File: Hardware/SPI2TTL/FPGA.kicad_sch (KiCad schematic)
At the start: 98 parts, among them J1 Conn_01x06, J7 Conn_02x07_Odd_Even, J8 Conn_01x40, SW1 SW_Push, SW2 SW_Push, SW3 SW_Push, SW4 SW_DIP_x03, U1 XC7S15-2CSGA225I, U2 IS25LP032D, X1 SG-5032CBN

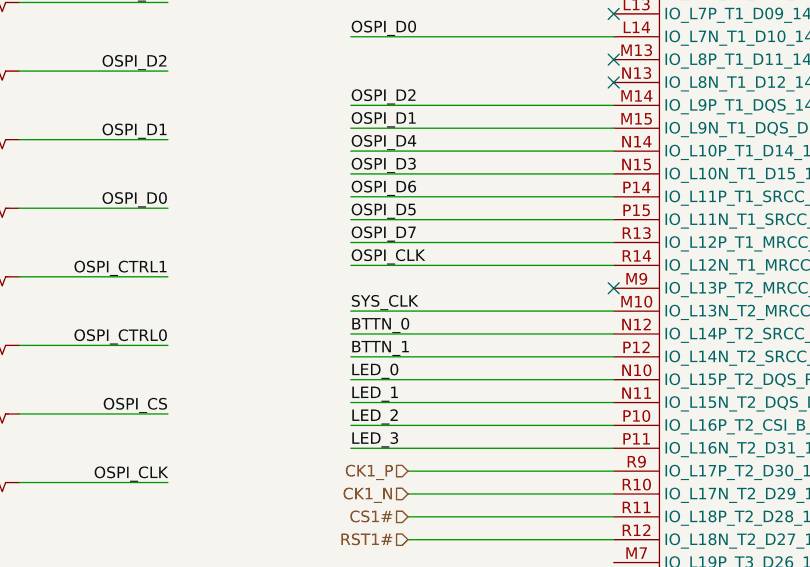
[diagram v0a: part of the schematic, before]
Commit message: Fixed CLK pins
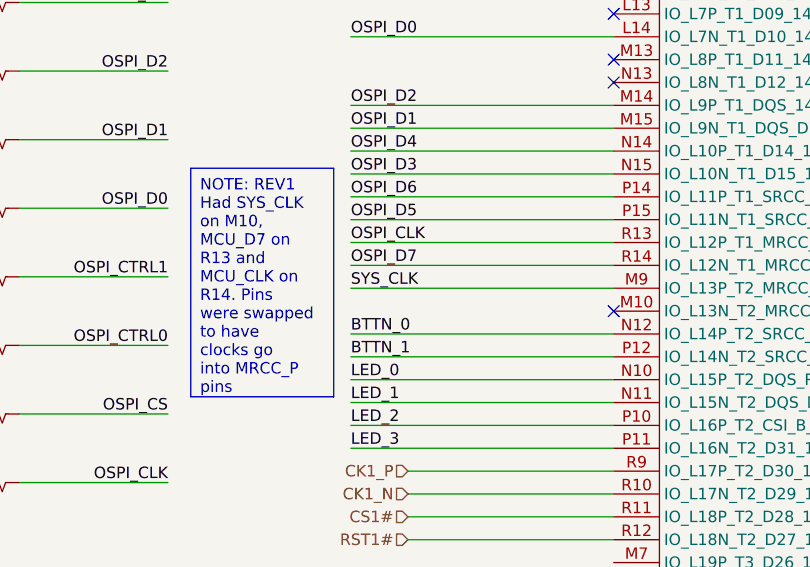
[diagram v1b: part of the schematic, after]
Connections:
- net OSPI_CLK: now also U1.R13 (IO_L12P_T1_MRCC_14); no longer U1.R14 (IO_L12N_T1_MRCC_14)
- net OSPI_D7: now also U1.R14 (IO_L12N_T1_MRCC_14); no longer U1.R13 (IO_L12P_T1_MRCC_14)
- net SYS_CLK: now also U1.M9 (IO_L13P_T2_MRCC_14); no longer U1.M10 (IO_L13N_T2_MRCC_14)
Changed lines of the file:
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@@
 	)
 	(no_connect
+		(at 132.08 106.68)
+	)
+	(no_connect
 		(at 506.73 176.53)
 	)
@@
 	)
 	(no_connect
-		(at 132.08 104.14)
-	)
-	(no_connect
 		(at 506.73 194.31)
 	)
@@
 	(wire
 		(pts
-			(xy 102.87 101.6) (xy 132.08 101.6)
-		)
-		(stroke
-			(width 0)
-			(type default)
-		)
-	)
-	(wire
-		(pts
 			(xy 476.25 81.28) (xy 476.25 78.74)
 		)
@@
 	(wire
 		(pts
-			(xy 102.87 99.06) (xy 132.08 99.06)
-		)
-		(stroke
-			(width 0)
-			(type default)
-		)
-	)
-	(wire
-		(pts
 			(xy 400.05 91.44) (xy 400.05 92.71)
 		)
@@
 	(wire
 		(pts
-			(xy 102.87 106.68) (xy 132.08 106.68)
-		)
-		(stroke
-			(width 0)
-			(type default)
-		)
-	)
-	(wire
-		(pts
 			(xy 476.25 96.52) (xy 478.79 96.52)
 		)
@@
 	(wire
 		(pts
+			(xy 102.87 104.14) (xy 132.08 104.14)
+		)
+		(stroke
+			(width 0)
+			(type default)
+		)
+	)
+	(wire
+		(pts
 			(xy 215.9 156.21) (xy 217.17 156.21)
 		)
@@
 	(wire
 		(pts
+			(xy 102.87 101.6) (xy 132.08 101.6)
+		)
+		(stroke
+			(width 0)
+			(type default)
+		)
+	)
+	(wire
+		(pts
 			(xy 240.03 44.45) (xy 245.11 44.45)
 		)
@@
 	(wire
 		(pts
+			(xy 102.87 99.06) (xy 132.08 99.06)
+		)
+		(stroke
+			(width 0)
+			(type default)
+		)
+	)
+	(wire
+		(pts
 			(xy 436.88 60.96) (xy 448.31 60.96)
 		)
@@
 		)
 	)
+	(text_box "NOTE: REV1 Had SYS_CLK on M10, MCU_D7 on R13 and MCU_CLK on R14. Pins were swapped to have clocks go into MRCC_P pins"
+		(exclude_from_sim no)
+		(at 85.09 90.805 0)
+		(size 15.875 25.4)
+		(stroke
+			(width 0)
+			(type default)
+		)
+		(fill
+			(type none)
+		)
+		(effects
+			(font
+				(size 1.27 1.27)
+			)
+			(justify left top)
+		)
+	)
 	(text_box "NOTE: Place 470nF Caps on VCCO Pins"
 		(exclude_from_sim no)
@@
 		)
 	)
+	(label "OSPI_CLK"
+		(at 102.87 99.06 0)
+		(fields_autoplaced yes)
+		(effects
+			(font
+				(size 1.27 1.27)
+			)
+			(justify left bottom)
+		)
+	)
 	(label "DISP_VSYNC"
 		(at 302.26 53.34 0)
@@
 		)
 	)
+	(label "SYS_CLK"
+		(at 102.87 104.14 0)
+		(fields_autoplaced yes)
+		(effects
+			(font
+				(size 1.27 1.27)
+			)
+			(justify left bottom)
+		)
+	)
 	(label "OSPI_D0"
 		(at 82.55 95.25 180)
@@
 		)
 	)
-	(label "OSPI_D7"
-		(at 102.87 99.06 0)
-		(fields_autoplaced yes)
-		(effects
-			(font
-				(size 1.27 1.27)
-			)
-			(justify left bottom)
-		)
-	)
 	(label "DISP_PWM"
 		(at 302.26 86.36 0)
@@
 		)
 	)
-	(label "OSPI_CLK"
-		(at 102.87 101.6 0)
-		(fields_autoplaced yes)
-		(effects
-			(font
-				(size 1.27 1.27)
-			)
-			(justify left bottom)
-		)
-	)
 	(label "TP_SDA"
 		(at 242.57 146.05 180)
@@
 		)
 	)
-	(label "DISP_D5"
-		(at 242.57 107.95 180)
+	(label "OSPI_D7"
+		(at 102.87 101.6 0)
 		(fields_autoplaced yes)
 		(effects
@@
 				(size 1.27 1.27)
 			)
-			(justify right bottom)
+			(justify left bottom)
 		)
 	)
-	(label "SYS_CLK"
-		(at 102.87 106.68 0)
+	(label "DISP_D5"
+		(at 242.57 107.95 180)
 		(fields_autoplaced yes)
 		(effects
@@
 				(size 1.27 1.27)
 			)
-			(justify left bottom)
+			(justify right bottom)
 		)
 	)
